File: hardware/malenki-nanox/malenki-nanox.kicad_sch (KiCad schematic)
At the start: 25 parts, among them J1 Conn_01x02_Male, J2 Conn_01x08_Male, J3 Conn_01x02, J5 Conn_01x02_Male, J6 Conn_01x02_Male, J7 Conn_01x02_Male, U1 A7105-MODULE, U2 AIC1734-33GUTR, U3 ATtiny1617-M, U5 DRV8837DSGR, U6 DRV8837DSGR, U7 DRV8837DSGR

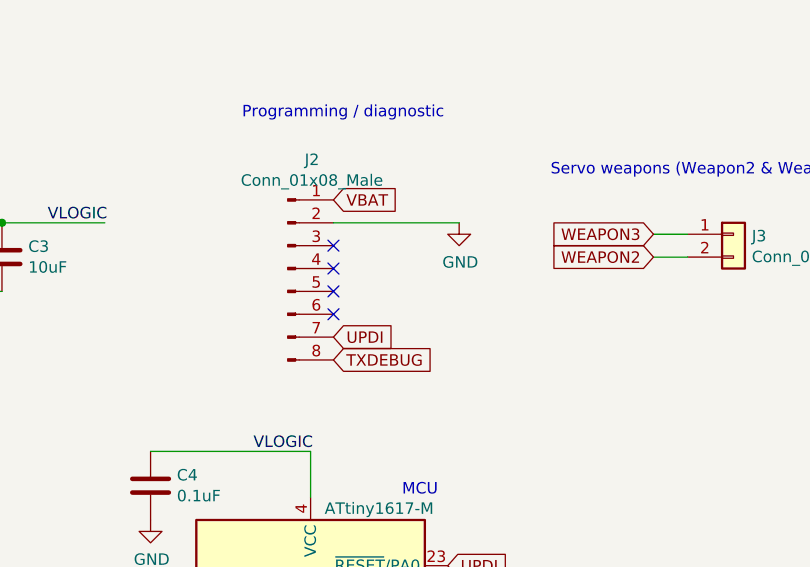
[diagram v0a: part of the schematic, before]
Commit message: Increase thermal relief on the pads for radio
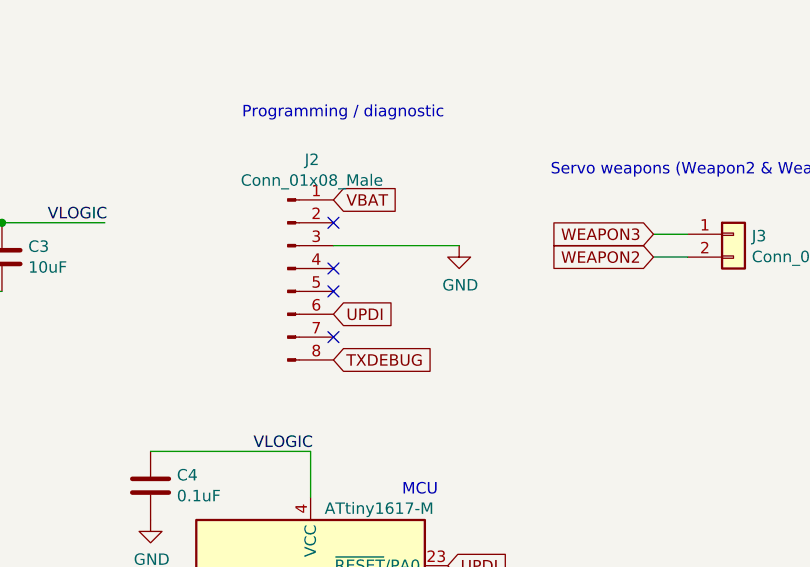
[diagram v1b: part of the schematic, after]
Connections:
- net GND: now also J2.3 (Pin_3); no longer J2.2 (Pin_2)
- net UPDI: now also J2.6 (Pin_6); no longer J2.7 (Pin_7)
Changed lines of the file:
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@@
   (junction (at 217.17 104.14))
   (junction (at 219.71 53.34))
+  (no_connect (at 129.54 55.88))
+  (no_connect (at 142.24 127))
+  (no_connect (at 142.24 119.38))
+  (no_connect (at 129.54 48.26))
+  (no_connect (at 129.54 60.96))
   (no_connect (at 142.24 124.46))
-  (no_connect (at 129.54 55.88))
+  (no_connect (at 38.1 140.97))
+  (no_connect (at 129.54 53.34))
   (no_connect (at 142.24 121.92))
-  (no_connect (at 142.24 127))
-  (no_connect (at 38.1 140.97))
-  (no_connect (at 142.24 119.38))
-  (no_connect (at 129.54 50.8))
-  (no_connect (at 129.54 53.34))
-  (no_connect (at 129.54 58.42))
   (wire (pts (xy 35.56 118.11) (xy 53.34 118.11)))
   (wire (pts (xy 38.1 48.26) (xy 57.15 48.26)))
@@
   (wire (pts (xy 127 73.66) (xy 109.22 73.66)))
   (wire (pts (xy 127 73.66) (xy 127 78.74)))
-  (wire (pts (xy 129.54 48.26) (xy 143.51 48.26)))
+  (wire (pts (xy 129.54 50.8) (xy 143.51 50.8)))
   (wire (pts (xy 165.1 49.53) (xy 168.91 49.53)))
   (wire (pts (xy 165.1 52.07) (xy 168.91 52.07)))
@@
     (effects (font (size 1.27 1.27)) (justify left))
   )
-  (global_label "UPDI" (shape input) (at 129.54 60.96 0)
+  (global_label "UPDI" (shape input) (at 129.54 58.42 0)
     (effects (font (size 1.27 1.27)) (justify left))
   )
@@
     )
   )
-  (symbol (lib_id "malenki-nano-rescue:GND-power") (at 143.51 48.26 0) (unit 1)
-    (property "Reference" "#PWR0104" (id 0) (at 143.51 54.61 0)
-      (effects (font (size 1.27 1.27)) hide)
-    )
-    (property "Value" "GND" (id 1) (at 143.637 52.6542 0))
-    (property "Footprint" "" (id 2) (at 143.51 48.26 0)
-      (effects (font (size 1.27 1.27)) hide)
-    )
-    (property "Datasheet" "" (id 3) (at 143.51 48.26 0)
-      (effects (font (size 1.27 1.27)) hide)
-    )
+  (symbol (lib_id "malenki-nano-rescue:GND-power") (at 143.51 50.8 0) (unit 1)
+    (property "Reference" "#PWR0104" (id 0) (at 143.51 57.15 0)
+      (effects (font (size 1.27 1.27)) hide)
+    )
+    (property "Value" "GND" (id 1) (at 143.637 55.1942 0))
+    (property "Footprint" "" (id 2) (at 143.51 50.8 0)
+      (effects (font (size 1.27 1.27)) hide)
+    )
+    (property "Datasheet" "" (id 3) (at 143.51 50.8 0)
+      (effects (font (size 1.27 1.27)) hide)
+    )
